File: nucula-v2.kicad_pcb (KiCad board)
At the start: 4 copper layers, 60 x 110 mm, 128 parts, among them J1 USB4105-GF-A-120, J2 JST-PH / 1S Li-ion, J3 KEYBOARD / USER FIT, J4 MAIN LINK / OPTIONAL, J5 MODULE LINK / OPTIONAL, Q1 IRLML6402, Q2 BSS138, Q3 IRLML6402, Q4 BSS138, Q5 BSS138, SW1 RESET, SW2 BOOT, U1 TP4054-42-SOT25R, U2 SY8089AAAC, U3 ESP32-C3-WROOM-02-N4, U4 USBLC6-2SC6, U5 TLV803EA30DBZR, U6 PN7160A1HN/C100E, U7 AP3012KTR-E1, U8 PCF8574T, U9 MCP1700T-3002E/TT, Y1 27.12MHz / CL 10pF

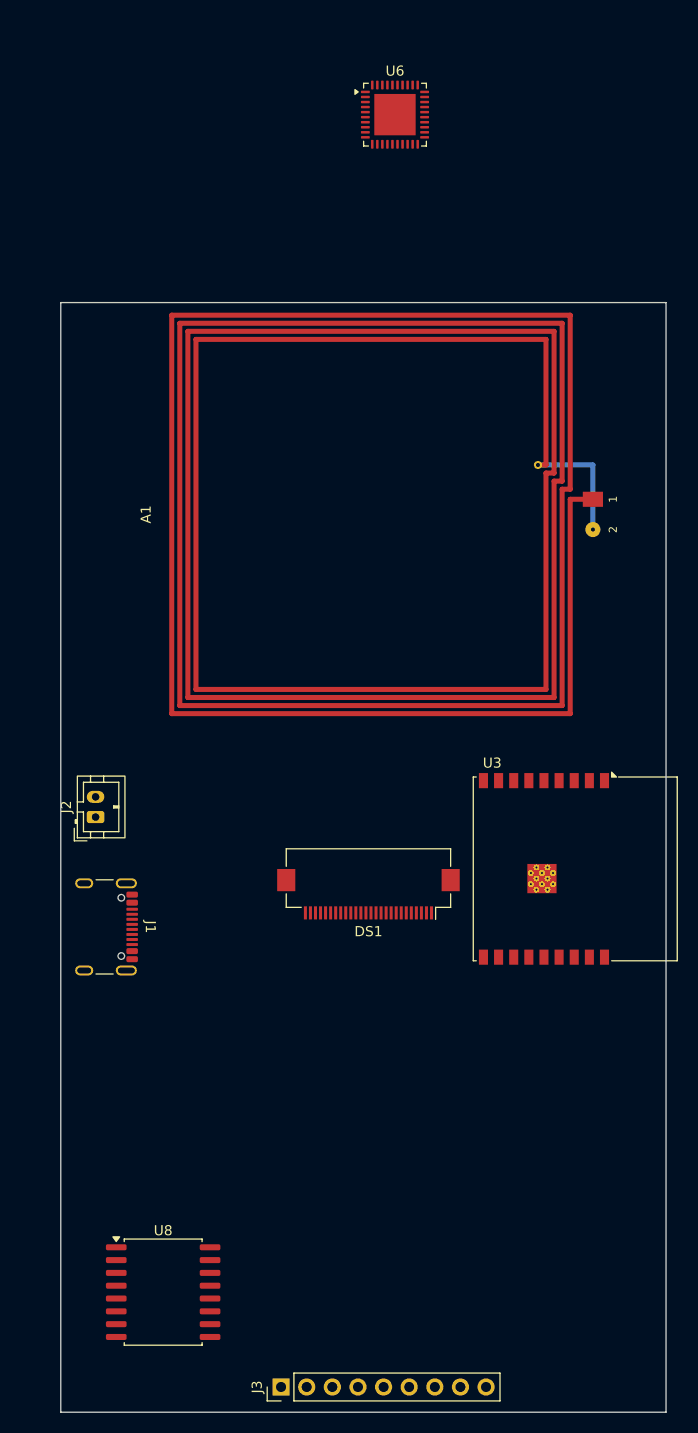
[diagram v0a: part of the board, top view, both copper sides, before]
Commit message: Add inside-feed NFC antenna and ESP antenna notch
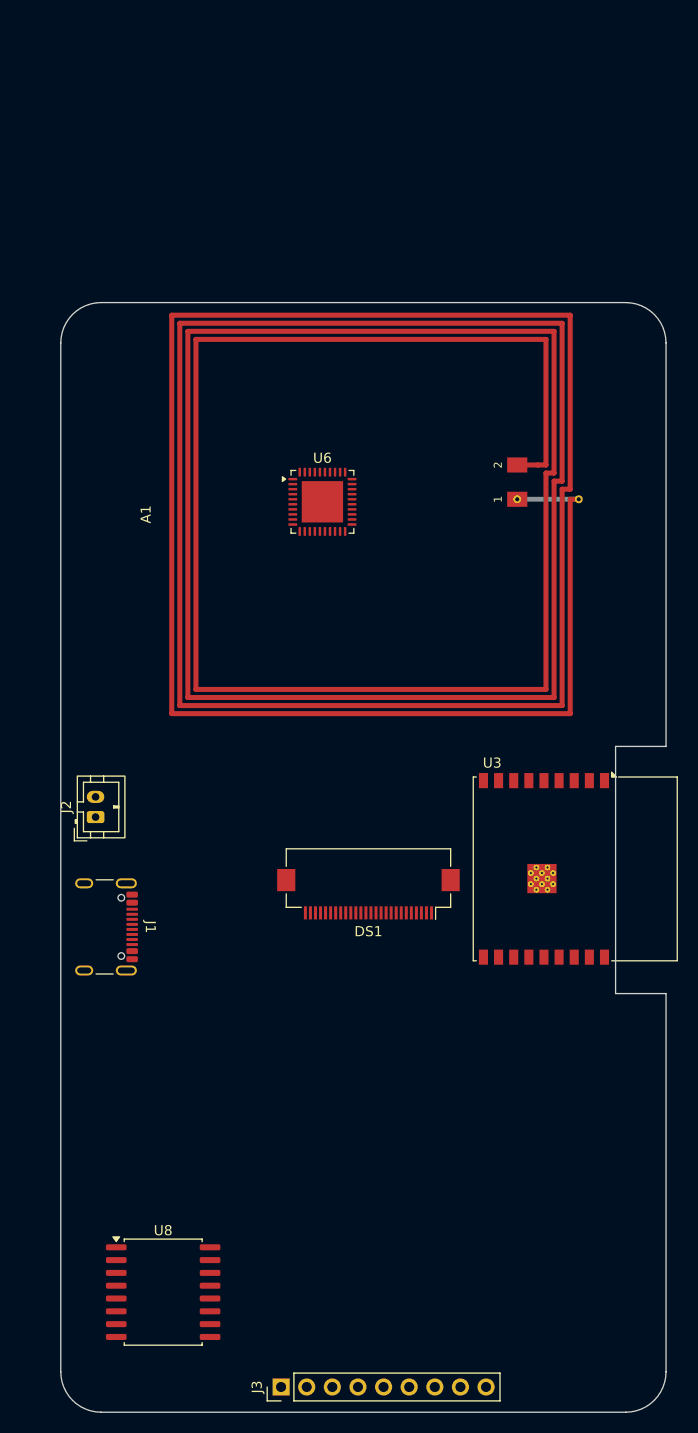
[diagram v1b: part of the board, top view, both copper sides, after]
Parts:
- A1: footprint Nucula_Project:NFC_PCB_Loop_40x40_4T_W0.50_S0.30 -> Nucula_Project:NFC_PCB_Loop_40x40_4T_W0.50_S0.30_InsideFeed
- moved U6 39.0 mm to (75.9, 69.8)
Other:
- outline, holes or cut-outs redrawn

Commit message: add break-away mouse bite line
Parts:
- added MB1: MouseBite_2Rows7_D0.60_P1.00_Inset_Gap2.00, Nucula_Project:MouseBite_2Rows7_D0.60_P1.00_Inset_Gap2.00, F.Cu at (62.0, 124.0)
- added MB2: MouseBite_2Rows7_D0.60_P1.00_Inset_Gap2.00, Nucula_Project:MouseBite_2Rows7_D0.60_P1.00_Inset_Gap2.00, F.Cu at (98.0, 124.0)
- J2: footprint Connector_JST:JST_PH_B2B-PH-K_1x02_P2.00mm_Vertical -> Nucula_Project:JST_PH_B2B-PH-SM4-TB_1x02-1MP_P2.00mm_Vertical
- moved R37 166.6 mm to (68.5, 149.5)
- moved C51 160.9 mm to (66.9, 141.5)
- moved R38 159.3 mm to (68.5, 144.5)
- moved R39 159.3 mm to (68.5, 147.0)
- moved C52 147.9 mm to (66.9, 138.5)
- moved J5 75.8 mm to (74.9, 130.0), turned to 90 degrees
- moved J4 56.2 mm to (74.9, 119.0), turned to 90 degrees
- moved J2 2.06 mm to (55.2, 100.0)
- moved J3 2.00 mm to (69.8, 157.5)
- moved DS1 0.50 mm to (80.0, 108.7)
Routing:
- net /KEY_INT_N: track 0.00 -> 14.4 mm
- net /+3V3: track 0.00 -> 14.4 mm
- net GND: track 0.00 -> 12.7 mm
- net /I2C_SCL: track 0.00 -> 12.7 mm
- net /I2C_SDA: track 0.00 -> 11.0 mm
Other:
- outline, holes or cut-outs redrawn
- board text added: "1 CUT BRIDGE"
- board text added: "2 SNAP"
- board text added: "35 mm KEYBOARD SECTION"
- board text added: "CUT CENTRAL BRIDGE BEFORE SNAPPING TABS"
- board text added: "KEYBOARD"

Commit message: commit again after save
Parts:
- moved J2 1.75 mm to (56.8, 100.9)
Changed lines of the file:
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@@
 	(footprint "Nucula_Project:JST_PH_B2B-PH-SM4-TB_1x02-1MP_P2.00mm_Vertical"
 		(layer "F.Cu")
-		(at 55.25 100 90)
+		(at 56.75 100.9 90)
 		(descr "JST PH series connector, B2B-PH-SM4-TB (http://www.jst-mfg.com/product/pdf/eng/ePH.pdf)")
 		(tags "connector JST PH vertical")

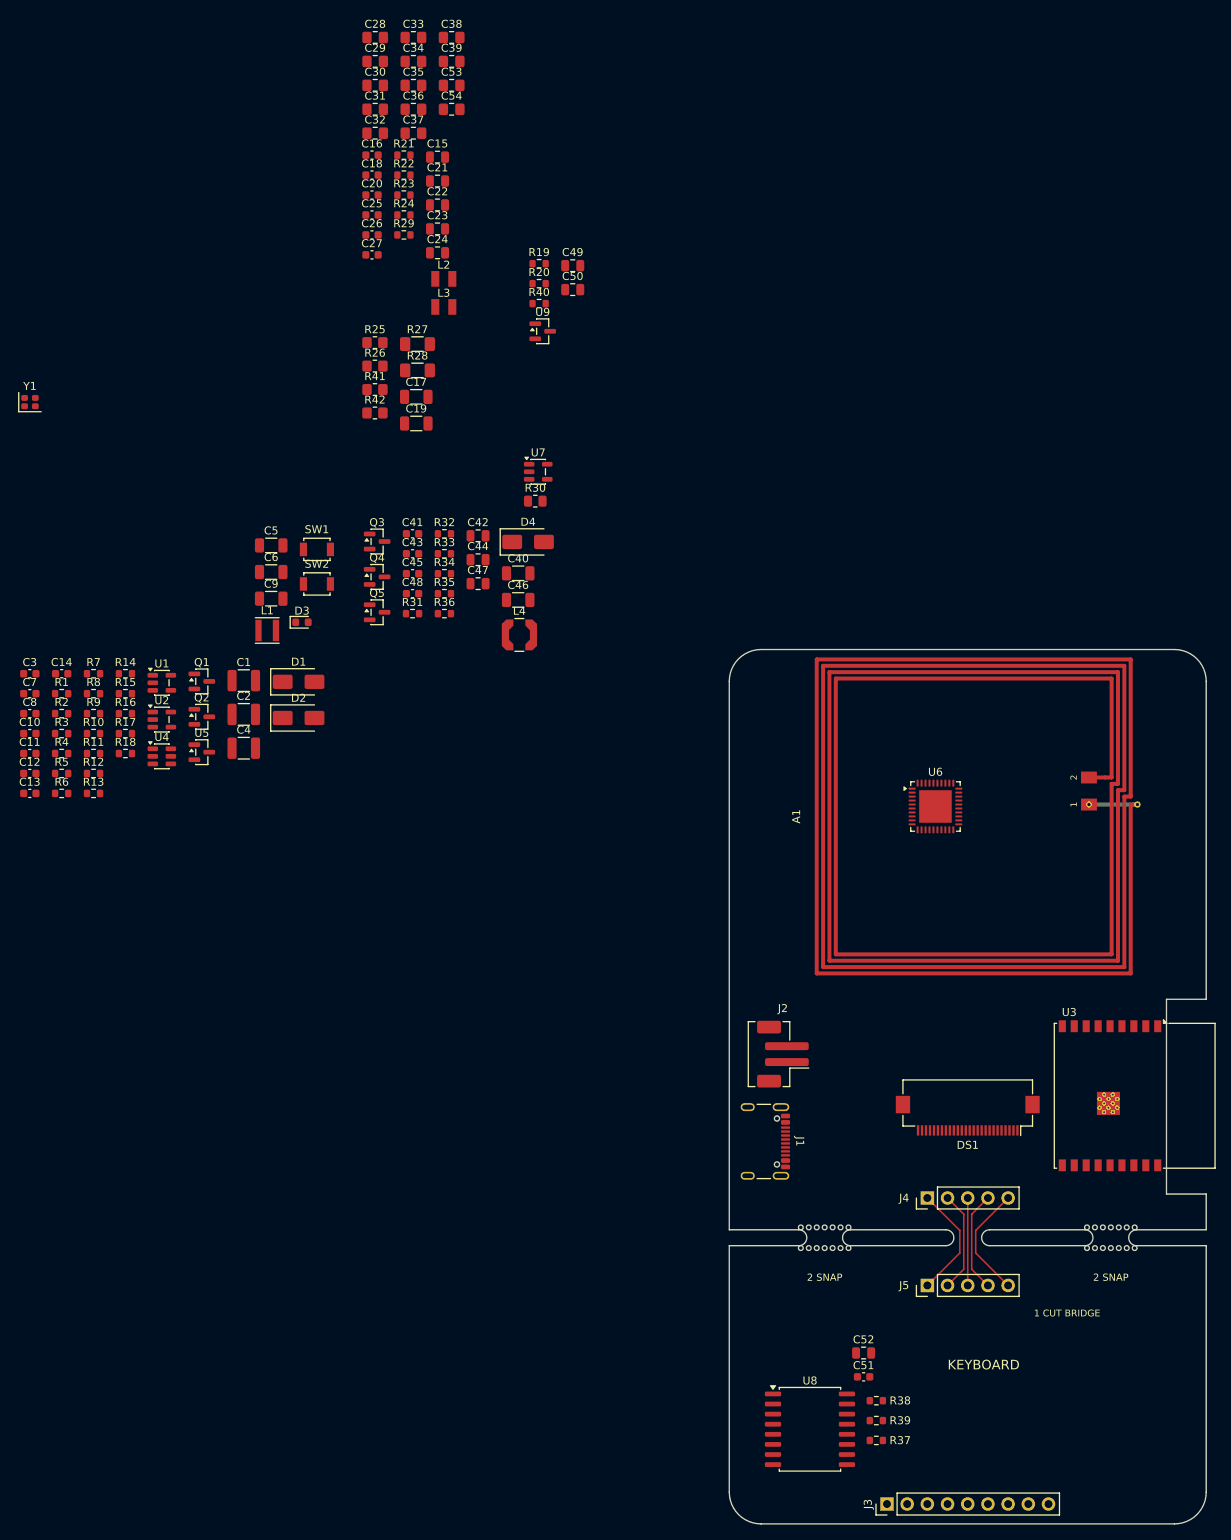
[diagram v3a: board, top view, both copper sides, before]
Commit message: Complete four-layer PCB placement and routing
Preserve fixed placements and route all 91 nets with top-side components, symmetric NFC matching branches, antenna pour exclusions, and power/USB routing rules. Set front and back solder mask to black.

Add layout drawings, validation tooling and reports, and explicit NFC antenna net labels. Validation records zero DRC errors, zero unconnected items, zero schematic parity findings, and 23 passing layout checks; two existing silkscreen-edge warnings remain documented.
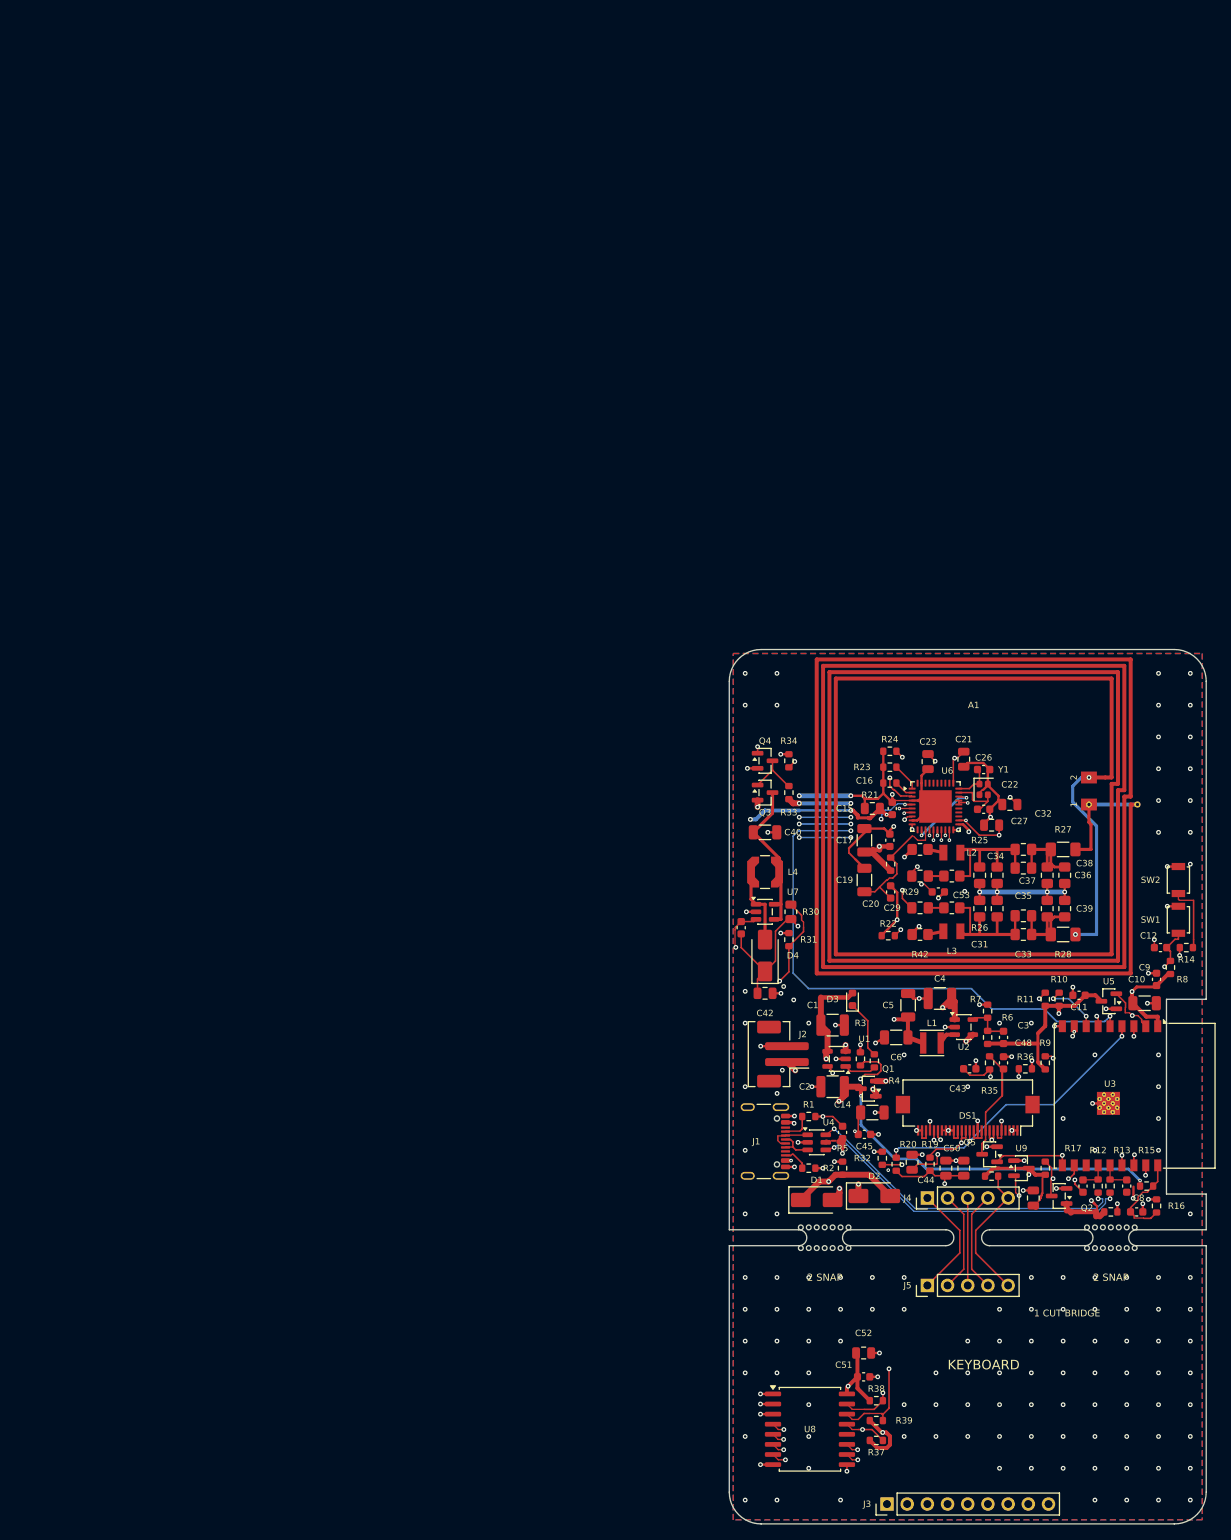
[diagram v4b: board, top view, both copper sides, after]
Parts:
- moved C8 150.3 mm to (100.0, 117.5), turned to -90 degrees
- moved C13 148.9 mm to (101.2, 120.8)
- moved C7 146.3 mm to (94.5, 117.5), turned to -90 degrees
- moved C10 145.1 mm to (103.8, 91.5), turned to 90 degrees
- moved C12 143.9 mm to (104.2, 87.5), turned to 180 degrees
- moved R16 143.7 mm to (103.8, 120.0), turned to 90 degrees
- moved R15 142.6 mm to (102.5, 117.5)
- moved R8 139.8 mm to (105.5, 90.0), turned to 90 degrees
- moved R14 137.8 mm to (107.5, 87.5)
- moved R13 137.1 mm to (97.9, 117.5), turned to 90 degrees
- moved R18 136.7 mm to (98.0, 120.8)
- moved R12 136.6 mm to (96.4, 117.5), turned to 90 degrees
- moved C33 136.5 mm to (87.0, 85.8)
- moved C11 135.5 mm to (94.0, 93.5), turned to 180 degrees
- moved C39 131.6 mm to (92.2, 82.6), turned to -90 degrees
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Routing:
- net /+3V3: track 14.4 -> 245.1 mm, vias 0 -> 10
- net GND: track 12.7 -> 235.3 mm, vias 0 -> 194
- net /I2C_SDA: track 11.0 -> 154.1 mm, vias 0 -> 8
- net /I2C_SCL: track 12.7 -> 153.9 mm, vias 0 -> 8
- net /VSYS: track 0.00 -> 128.3 mm, vias 0 -> 11
- net /OLED_PWR_EN: track 0.00 -> 120.3 mm, vias 0 -> 4
- net /NFC_VEN: track 0.00 -> 98.2 mm, vias 0 -> 6
- net /NFC_IRQ: track 0.00 -> 77.5 mm, vias 0 -> 3
- net /Power + ESP32-C3/VBUS: track 0.00 -> 64.5 mm, vias 0 -> 5
- net /Power + ESP32-C3/VBAT: track 0.00 -> 64.4 mm, vias 0 -> 5
- net /OLED / SSD1309 / 0x3C/OLED_12V5: track 0.00 -> 61.6 mm, vias 0 -> 3
- net /Power + ESP32-C3/USB_5V: track 0.00 -> 52.7 mm, vias 0 -> 3
- net /+3V0: track 0.00 -> 50.9 mm, vias 0 -> 4
- net /KEY_INT_N: track 14.4 -> 59.8 mm, vias 0 -> 2
- net /Power + ESP32-C3/USB_ESD_D+: track 0.00 -> 41.5 mm, vias 0 -> 2
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- added copper zone on B.Cu, net GND
- added copper zone on F.Cu, net GND
- added copper zone on In1.Cu, net GND
- added copper zone on In2.Cu, net GND
